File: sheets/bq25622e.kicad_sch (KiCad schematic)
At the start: 16 parts, among them U1 BQ25628E

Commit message: More cleanup
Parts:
- renumbered C1 to C13, C3 to C14, C4 to C15, C6 to C16, C9 to C17, C10 to C18, C12 to C19, LED1 to LED2, R1 to R12, R2 to R13, R3 to R14, R8 to R15, R9 to R16, R11 to R17, U1 to U4
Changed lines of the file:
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@@
 		(on_board yes)
 		(dnp no)
-		(property "Reference" "C9"
+		(property "Reference" "C17"
 			(at 121.412 54.737 90)
 			(effects
@@
 		(instances
 			(project "esp32s3-powerfeather"
-				(path "/5be6a852-fa78-49fa-bb8c-8d5ad39f4b26/46173bec-ea31-4af7-a417-264e4953a5cb/1dd60fd9-c406-4047-80b6-6321e22f9725"
-					(reference "C9")
+				(path "/5be6a852-fa78-49fa-bb8c-8d5ad39f4b26/a940761a-0d45-4491-ba89-ec093a8f239f/1dd60fd9-c406-4047-80b6-6321e22f9725"
+					(reference "C17")
 					(unit 1)
 				)
@@
 		(dnp no)
 		(fields_autoplaced yes)
-		(property "Reference" "U1"
+		(property "Reference" "U4"
 			(at 102.9335 42.418 0)
 			(effects
@@
 		(instances
 			(project "esp32s3-powerfeather"
-				(path "/5be6a852-fa78-49fa-bb8c-8d5ad39f4b26/46173bec-ea31-4af7-a417-264e4953a5cb/1dd60fd9-c406-4047-80b6-6321e22f9725"
-					(reference "U1")
+				(path "/5be6a852-fa78-49fa-bb8c-8d5ad39f4b26/a940761a-0d45-4491-ba89-ec093a8f239f/1dd60fd9-c406-4047-80b6-6321e22f9725"
+					(reference "U4")
 					(unit 1)
 				)
@@
 		(on_board yes)
 		(dnp no)
-		(property "Reference" "C6"
+		(property "Reference" "C16"
 			(at 111.506 84.328 0)
 			(effects
@@
 		(instances
 			(project "esp32s3-powerfeather"
-				(path "/5be6a852-fa78-49fa-bb8c-8d5ad39f4b26/46173bec-ea31-4af7-a417-264e4953a5cb/1dd60fd9-c406-4047-80b6-6321e22f9725"
-					(reference "C6")
+				(path "/5be6a852-fa78-49fa-bb8c-8d5ad39f4b26/a940761a-0d45-4491-ba89-ec093a8f239f/1dd60fd9-c406-4047-80b6-6321e22f9725"
+					(reference "C16")
 					(unit 1)
 				)
@@
 		(on_board yes)
 		(dnp no)
-		(property "Reference" "R1"
+		(property "Reference" "R12"
 			(at 59.69 66.04 0)
 			(effects
@@
 		(instances
 			(project "esp32s3-powerfeather"
-				(path "/5be6a852-fa78-49fa-bb8c-8d5ad39f4b26/46173bec-ea31-4af7-a417-264e4953a5cb/1dd60fd9-c406-4047-80b6-6321e22f9725"
-					(reference "R1")
+				(path "/5be6a852-fa78-49fa-bb8c-8d5ad39f4b26/a940761a-0d45-4491-ba89-ec093a8f239f/1dd60fd9-c406-4047-80b6-6321e22f9725"
+					(reference "R12")
 					(unit 1)
 				)
@@
 		(on_board yes)
 		(dnp no)
-		(property "Reference" "R3"
+		(property "Reference" "R14"
 			(at 74.93 60.198 90)
 			(effects
@@
 		(instances
 			(project "esp32s3-powerfeather"
-				(path "/5be6a852-fa78-49fa-bb8c-8d5ad39f4b26/46173bec-ea31-4af7-a417-264e4953a5cb/1dd60fd9-c406-4047-80b6-6321e22f9725"
-					(reference "R3")
+				(path "/5be6a852-fa78-49fa-bb8c-8d5ad39f4b26/a940761a-0d45-4491-ba89-ec093a8f239f/1dd60fd9-c406-4047-80b6-6321e22f9725"
+					(reference "R14")
 					(unit 1)
 				)
@@
 		(instances
 			(project "esp32s3-powerfeather"
-				(path "/5be6a852-fa78-49fa-bb8c-8d5ad39f4b26/46173bec-ea31-4af7-a417-264e4953a5cb/1dd60fd9-c406-4047-80b6-6321e22f9725"
+				(path "/5be6a852-fa78-49fa-bb8c-8d5ad39f4b26/a940761a-0d45-4491-ba89-ec093a8f239f/1dd60fd9-c406-4047-80b6-6321e22f9725"
 					(reference "L1")
 					(unit 1)
@@
 		(on_board yes)
 		(dnp no)
-		(property "Reference" "C12"
+		(property "Reference" "C19"
 			(at 138.43 74.93 0)
 			(effects
@@
 		(instances
 			(project "esp32s3-powerfeather"
-				(path "/5be6a852-fa78-49fa-bb8c-8d5ad39f4b26/46173bec-ea31-4af7-a417-264e4953a5cb/1dd60fd9-c406-4047-80b6-6321e22f9725"
-					(reference "C12")
+				(path "/5be6a852-fa78-49fa-bb8c-8d5ad39f4b26/a940761a-0d45-4491-ba89-ec093a8f239f/1dd60fd9-c406-4047-80b6-6321e22f9725"
+					(reference "C19")
 					(unit 1)
 				)
@@
 		(on_board yes)
 		(dnp no)
-		(property "Reference" "R2"
+		(property "Reference" "R13"
 			(at 74.168 48.26 0)
 			(effects
@@
 		(instances
 			(project "esp32s3-powerfeather"
-				(path "/5be6a852-fa78-49fa-bb8c-8d5ad39f4b26/46173bec-ea31-4af7-a417-264e4953a5cb/1dd60fd9-c406-4047-80b6-6321e22f9725"
-					(reference "R2")
+				(path "/5be6a852-fa78-49fa-bb8c-8d5ad39f4b26/a940761a-0d45-4491-ba89-ec093a8f239f/1dd60fd9-c406-4047-80b6-6321e22f9725"
+					(reference "R13")
 					(unit 1)
 				)
@@
 		(on_board yes)
 		(dnp no)
-		(property "Reference" "LED1"
+		(property "Reference" "LED2"
 			(at 59.055 46.99 0)
 			(effects
@@
 		(instances
 			(project "esp32s3-powerfeather"
-				(path "/5be6a852-fa78-49fa-bb8c-8d5ad39f4b26/46173bec-ea31-4af7-a417-264e4953a5cb/1dd60fd9-c406-4047-80b6-6321e22f9725"
-					(reference "LED1")
+				(path "/5be6a852-fa78-49fa-bb8c-8d5ad39f4b26/a940761a-0d45-4491-ba89-ec093a8f239f/1dd60fd9-c406-4047-80b6-6321e22f9725"
+					(reference "LED2")
 					(unit 1)
 				)
@@
 		(on_board yes)
 		(dnp no)
-		(property "Reference" "C1"
+		(property "Reference" "C13"
 			(at 62.23 85.09 0)
 			(effects
@@
 		(instances
 			(project "esp32s3-powerfeather"
-				(path "/5be6a852-fa78-49fa-bb8c-8d5ad39f4b26/46173bec-ea31-4af7-a417-264e4953a5cb/1dd60fd9-c406-4047-80b6-6321e22f9725"
-					(reference "C1")
+				(path "/5be6a852-fa78-49fa-bb8c-8d5ad39f4b26/a940761a-0d45-4491-ba89-ec093a8f239f/1dd60fd9-c406-4047-80b6-6321e22f9725"
+					(reference "C13")
 					(unit 1)
 				)
@@
 		(on_board yes)
 		(dnp no)
-		(property "Reference" "#PWR016"
+		(property "Reference" "#PWR033"
 			(at 129.54 55.88 0)
 			(effects
@@
 		(instances
 			(project "esp32s3-powerfeather"
-				(path "/5be6a852-fa78-49fa-bb8c-8d5ad39f4b26/46173bec-ea31-4af7-a417-264e4953a5cb/1dd60fd9-c406-4047-80b6-6321e22f9725"
-					(reference "#PWR016")
+				(path "/5be6a852-fa78-49fa-bb8c-8d5ad39f4b26/a940761a-0d45-4491-ba89-ec093a8f239f/1dd60fd9-c406-4047-80b6-6321e22f9725"
+					(reference "#PWR033")
 					(unit 1)
 				)
@@
 		(on_board yes)
 		(dnp no)
-		(property "Reference" "R8"
+		(property "Reference" "R15"
 			(at 125.73 60.96 90)
 			(effects
@@
 		(instances
 			(project "esp32s3-powerfeather"
-				(path "/5be6a852-fa78-49fa-bb8c-8d5ad39f4b26/46173bec-ea31-4af7-a417-264e4953a5cb/1dd60fd9-c406-4047-80b6-6321e22f9725"
-					(reference "R8")
+				(path "/5be6a852-fa78-49fa-bb8c-8d5ad39f4b26/a940761a-0d45-4491-ba89-ec093a8f239f/1dd60fd9-c406-4047-80b6-6321e22f9725"
+					(reference "R15")
 					(unit 1)
 				)
@@
 		(on_board yes)
 		(dnp no)
-		(property "Reference" "#PWR012"
+		(property "Reference" "#PWR032"
 			(at 86.36 50.8 0)
 			(effects
@@
 		(instances
 			(project "esp32s3-powerfeather"
-				(path "/5be6a852-fa78-49fa-bb8c-8d5ad39f4b26/46173bec-ea31-4af7-a417-264e4953a5cb/1dd60fd9-c406-4047-80b6-6321e22f9725"
-					(reference "#PWR012")
+				(path "/5be6a852-fa78-49fa-bb8c-8d5ad39f4b26/a940761a-0d45-4491-ba89-ec093a8f239f/1dd60fd9-c406-4047-80b6-6321e22f9725"
+					(reference "#PWR032")
 					(unit 1)
 				)
@@
 		(on_board yes)
 		(dnp no)
-		(property "Reference" "C3"
+		(property "Reference" "C14"
 			(at 90.17 85.09 0)
 			(effects
@@
 		(instances
 			(project "esp32s3-powerfeather"
-				(path "/5be6a852-fa78-49fa-bb8c-8d5ad39f4b26/46173bec-ea31-4af7-a417-264e4953a5cb/1dd60fd9-c406-4047-80b6-6321e22f9725"
-					(reference "C3")
+				(path "/5be6a852-fa78-49fa-bb8c-8d5ad39f4b26/a940761a-0d45-4491-ba89-ec093a8f239f/1dd60fd9-c406-4047-80b6-6321e22f9725"
+					(reference "C14")
 					(unit 1)
 				)
@@
 		(on_board yes)
 		(dnp no)
-		(property "Reference" "R9"
+		(property "Reference" "R16"
 			(at 131.064 73.152 0)
 			(effects
@@
 		(instances
 			(project "esp32s3-powerfeather"
-				(path "/5be6a852-fa78-49fa-bb8c-8d5ad39f4b26/46173bec-ea31-4af7-a417-264e4953a5cb/1dd60fd9-c406-4047-80b6-6321e22f9725"
-					(reference "R9")
+				(path "/5be6a852-fa78-49fa-bb8c-8d5ad39f4b26/a940761a-0d45-4491-ba89-ec093a8f239f/1dd60fd9-c406-4047-80b6-6321e22f9725"
+					(reference "R16")
 					(unit 1)
 				)
@@
 		(on_board yes)
 		(dnp no)
-		(property "Reference" "R11"
+		(property "Reference" "R17"
 			(at 125.73 85.725 0)
 			(effects
@@
 		(instances
 			(project "esp32s3-powerfeather"
-				(path "/5be6a852-fa78-49fa-bb8c-8d5ad39f4b26/46173bec-ea31-4af7-a417-264e4953a5cb/1dd60fd9-c406-4047-80b6-6321e22f9725"
-					(reference "R11")
+				(path "/5be6a852-fa78-49fa-bb8c-8d5ad39f4b26/a940761a-0d45-4491-ba89-ec093a8f239f/1dd60fd9-c406-4047-80b6-6321e22f9725"
+					(reference "R17")
 					(unit 1)
 				)
@@
 		(on_board yes)
 		(dnp no)
-		(property "Reference" "C4"
+		(property "Reference" "C15"
 			(at 92.202 38.862 0)
 			(effects
@@
 		(instances
 			(project "esp32s3-powerfeather"
-				(path "/5be6a852-fa78-49fa-bb8c-8d5ad39f4b26/46173bec-ea31-4af7-a417-264e4953a5cb/1dd60fd9-c406-4047-80b6-6321e22f9725"
-					(reference "C4")
+				(path "/5be6a852-fa78-49fa-bb8c-8d5ad39f4b26/a940761a-0d45-4491-ba89-ec093a8f239f/1dd60fd9-c406-4047-80b6-6321e22f9725"
+					(reference "C15")
 					(unit 1)
 				)
@@
 		(on_board yes)
 		(dnp no)
-		(property "Reference" "C10"
+		(property "Reference" "C18"
 			(at 122.555 46.99 90)
 			(effects
@@
 		(instances
 			(project "esp32s3-powerfeather"
-				(path "/5be6a852-fa78-49fa-bb8c-8d5ad39f4b26/46173bec-ea31-4af7-a417-264e4953a5cb/1dd60fd9-c406-4047-80b6-6321e22f9725"
-					(reference "C10")
-					(unit 1)
-				)
+				(path "/5be6a852-fa78-49fa-bb8c-8d5ad39f4b26/a940761a-0d45-4491-ba89-ec093a8f239f/1dd60fd9-c406-4047-80b6-6321e22f9725"
+					(reference "C18")
+					(unit 1)
+				)

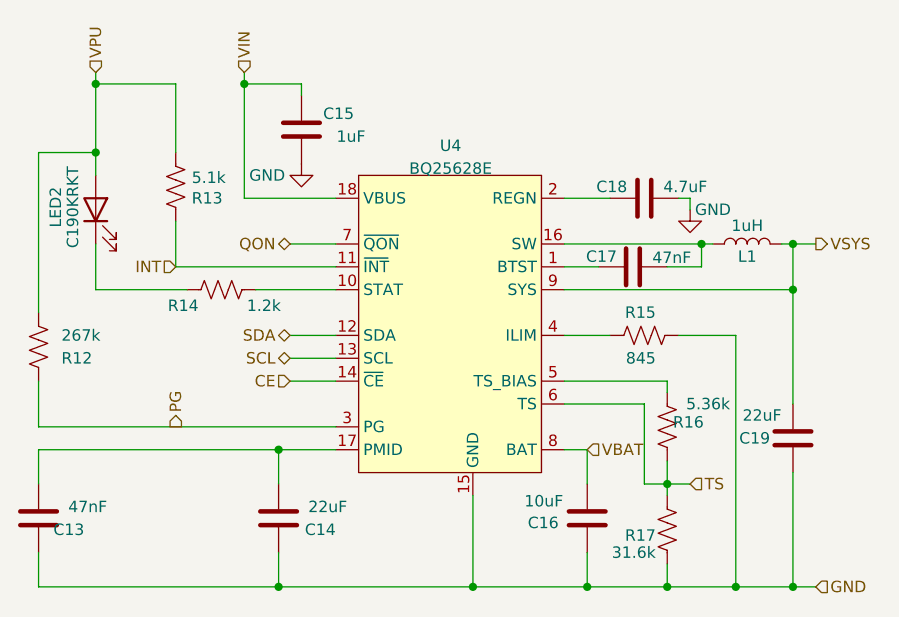
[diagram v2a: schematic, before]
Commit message: Bring out ILIM
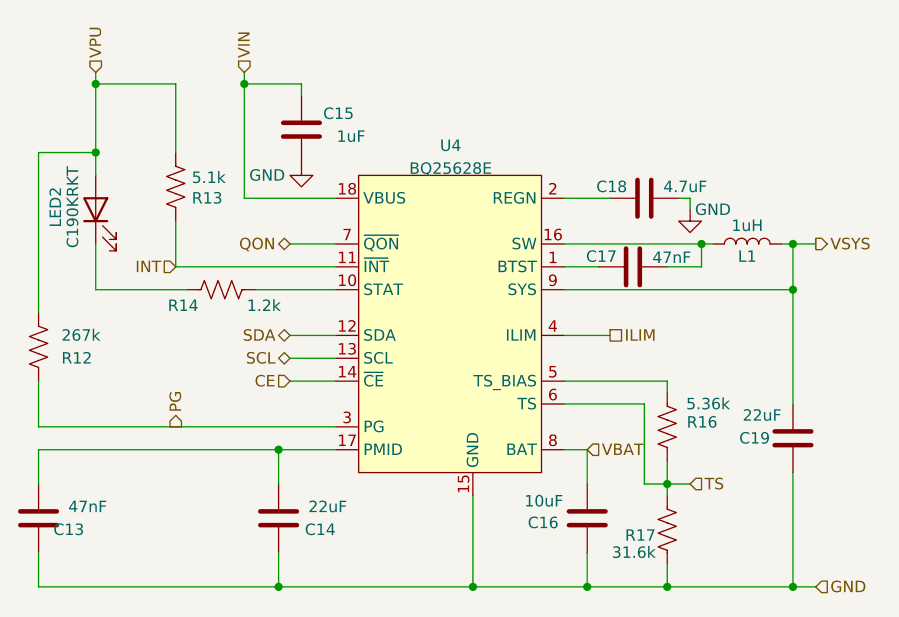
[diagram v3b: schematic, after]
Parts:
- removed R15: 845, Resistor_SMD:R_0402_1005Metric, symbol Device:R_US
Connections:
- net ILIM: now reaches U4.4 (ILIM)
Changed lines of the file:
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@@
-	)
-	(junction
-		(at 134.62 91.44)
-		(diameter 0)
-		(color 0 0 0 0)
 	)
 	(junction
@@
 	(wire
 		(pts
-			(xy 134.62 91.44) (xy 140.97 91.44)
-		)
-		(stroke
-			(width 0)
-			(type default)
-		)
-	)
-	(wire
-		(pts
 			(xy 83.82 76.2) (xy 83.82 80.01)
 		)
@@
 	(wire
 		(pts
-			(xy 134.62 63.5) (xy 134.62 91.44)
-		)
-		(stroke
-			(width 0)
-			(type default)
-		)
-	)
-	(wire
-		(pts
 			(xy 140.97 78.74) (xy 140.97 91.44)
 		)
@@
 	(wire
 		(pts
-			(xy 128.27 63.5) (xy 134.62 63.5)
-		)
-		(stroke
-			(width 0)
-			(type default)
-		)
-	)
-	(wire
-		(pts
 			(xy 115.57 63.5) (xy 120.65 63.5)
 		)
@@
 	(wire
 		(pts
-			(xy 127 91.44) (xy 134.62 91.44)
+			(xy 127 91.44) (xy 140.97 91.44)
 		)
 		(stroke
@@
 		)
 	)
+	(hierarchical_label "ILIM"
+		(shape passive)
+		(at 120.65 63.5 0)
+		(fields_autoplaced yes)
+		(effects
+			(font
+				(size 1.27 1.27)
+			)
+			(justify left)
+		)
+	)
 	(hierarchical_label "INT"
 		(shape input)
@@
 	)
 	(symbol
-		(lib_id "Device:R_US")
-		(at 124.46 63.5 90)
-		(unit 1)
-		(exclude_from_sim no)
-		(in_bom yes)
-		(on_board yes)
-		(dnp no)
-		(property "Reference" "R15"
-			(at 125.73 60.96 90)
-			(effects
-				(font
-					(size 1.27 1.27)
-				)
-				(justify left)
-			)
-		)
-		(property "Value" "845"
-			(at 125.73 66.04 90)
-			(effects
-				(font
-					(size 1.27 1.27)
-				)
-				(justify left)
-			)
-		)
-		(property "Footprint" "Resistor_SMD:R_0402_1005Metric"
-			(at 124.714 62.484 90)
-			(effects
-				(font
-					(size 1.27 1.27)
-				)
-				(hide yes)
-			)
-		)
-		(property "Datasheet" "https://www.mouser.ph/datasheet/2/447/PYu_AC_51_RoHS_L_9-3005297.pdf"
-			(at 124.46 63.5 0)
-			(effects
-				(font
-					(size 1.27 1.27)
-				)
-				(hide yes)
-			)
-		)
-		(property "Description" ""
-			(at 124.46 63.5 0)
-			(effects
-				(font
-					(size 1.27 1.27)
-				)
-				(hide yes)
-			)
-		)
-		(property "MPN" "603-AC0402FR-07845RL"
-			(at 124.46 63.5 0)
-			(effects
-				(font
-					(size 1.27 1.27)
-				)
-				(hide yes)
-			)
-		)
-		(pin "1"
-		)
-		(pin "2"
-		)
-		(instances
-			(project "esp32s3-powerfeather"
-				(path "/5be6a852-fa78-49fa-bb8c-8d5ad39f4b26/a940761a-0d45-4491-ba89-ec093a8f239f/1dd60fd9-c406-4047-80b6-6321e22f9725"
-					(reference "R15")
-					(unit 1)
-				)
-			)
-		)
-	)
-	(symbol
 		(lib_id "power:GND")
 		(at 86.36 44.45 0)
@@
 		(dnp no)
 		(property "Reference" "R16"
-			(at 131.064 73.152 0)
-			(effects
-				(font
+			(at 132.588 73.152 0)
+			(effects
+				(font
